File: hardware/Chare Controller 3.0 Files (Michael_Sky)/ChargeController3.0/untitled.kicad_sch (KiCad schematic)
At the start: 2 parts, among them J1 Conn_02x26_Odd_Even, J12 Conn_02x26_Odd_Even

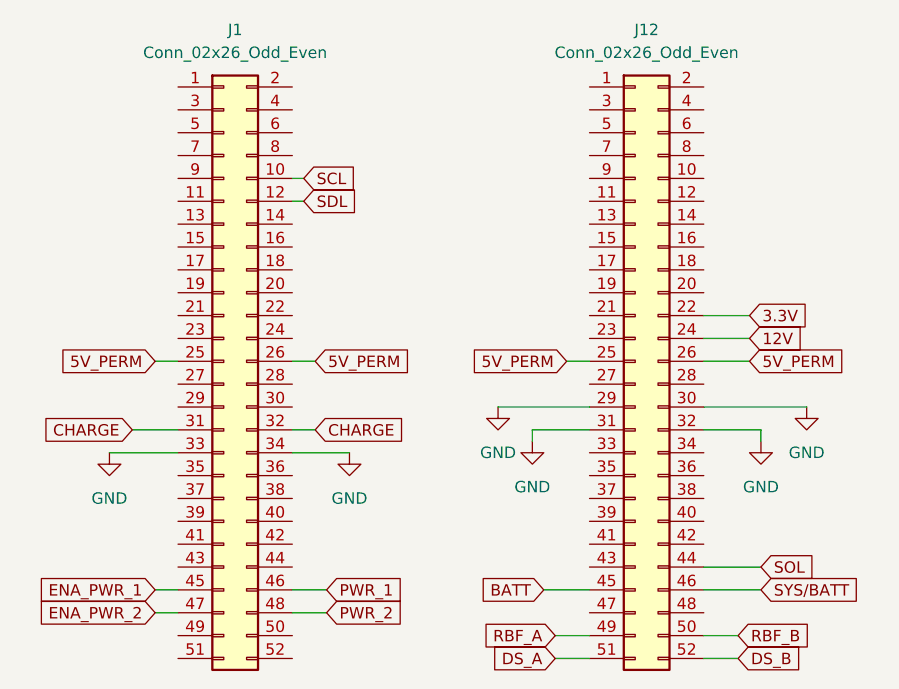
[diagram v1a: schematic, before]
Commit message: added pins and pcb template
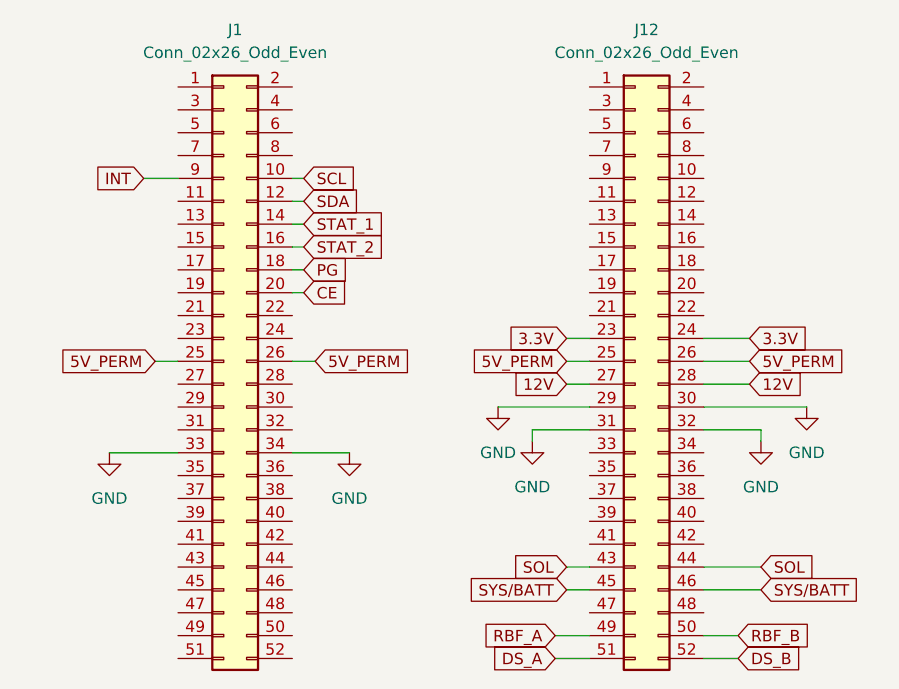
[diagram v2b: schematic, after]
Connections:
- net BATT is gone; now on net SYS/BATT: J12.45 (Pin_45)
- net 12V: now also J12.27 (Pin_27), J12.28 (Pin_28); no longer J12.24 (Pin_24)
- net 3.3V: now also J12.23 (Pin_23), J12.24 (Pin_24); no longer J12.22 (Pin_22)
- net SOL: now also J12.43 (Pin_43)
- net STAT_1: now reaches J1.14 (Pin_14)
- net STAT_2: now reaches J1.16 (Pin_16)
- net PG: now reaches J1.18 (Pin_18)
- net CE: now reaches J1.20 (Pin_20)
- net INT: now reaches J1.9 (Pin_9)
- net CHARGE: no longer names the net of J1.31 (Pin_31)
- net CHARGE: no longer J1.32 (Pin_32)
- net ENA_PWR_1: no longer names the net of J1.45 (Pin_45)
- net ENA_PWR_2: no longer names the net of J1.47 (Pin_47)
- net PWR_1: no longer names the net of J1.46 (Pin_46)
- net PWR_2: no longer names the net of J1.48 (Pin_48)
- net SDL renamed SDA
